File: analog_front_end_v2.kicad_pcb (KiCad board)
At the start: 4 copper layers, 153 parts, among them J1 Conn_Coaxial, J3 Conn_01x01_Socket, J4 Conn_01x01_Socket, U1 ADL5531, U10 PMOD 2x6, U11 LP2985-5.0, U12 LP2985-5.0, U13 LT1363, U14 MAX 735, U15 LP2985-2.5, U16 MAX889SESA, U17 MAX6102, U2 ADL5531, U3 ADL5531, U4 PE4140B-Z, U5 ADF4360-9, U6 LTC1406, U7 THS4551, U8 LT1363, U9 PMOD 2x6

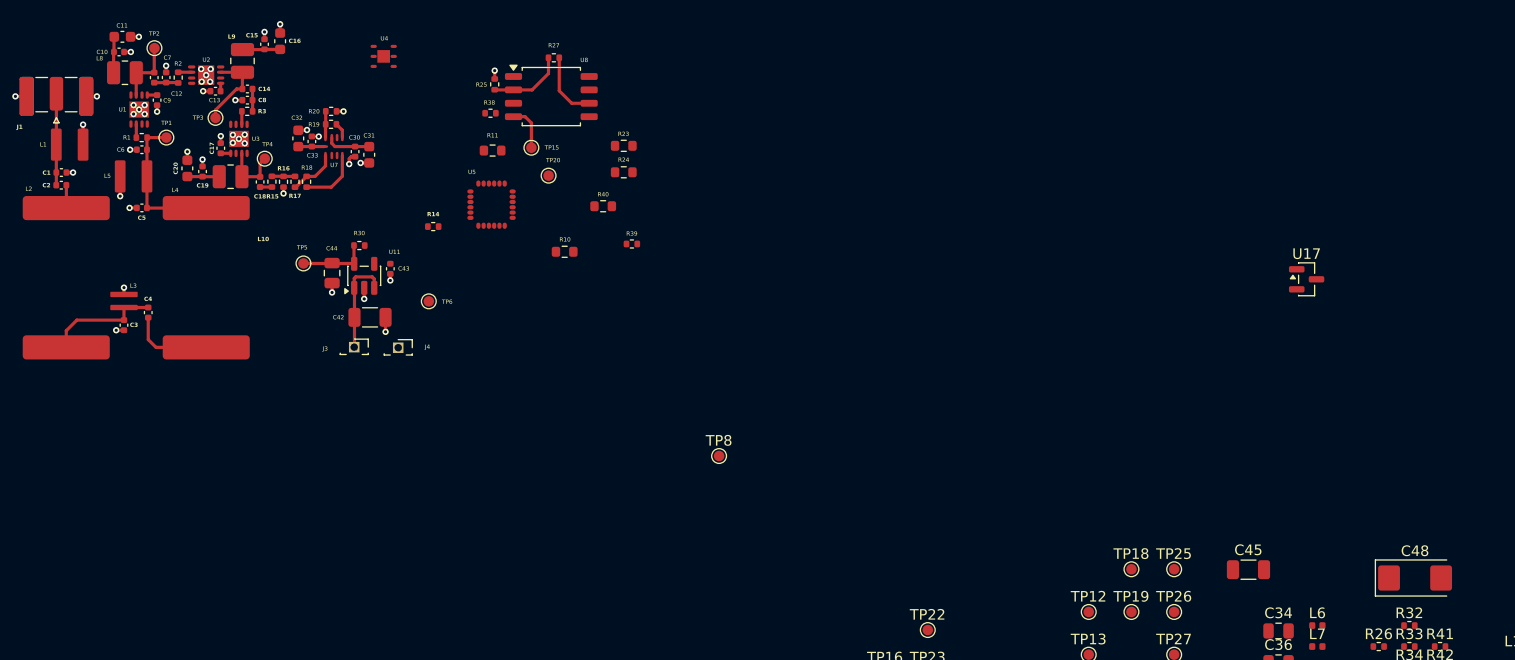
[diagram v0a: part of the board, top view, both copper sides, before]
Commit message: Routing for 5V_LNA and VIN connections. Also added note to add GND Planes for L2/L2
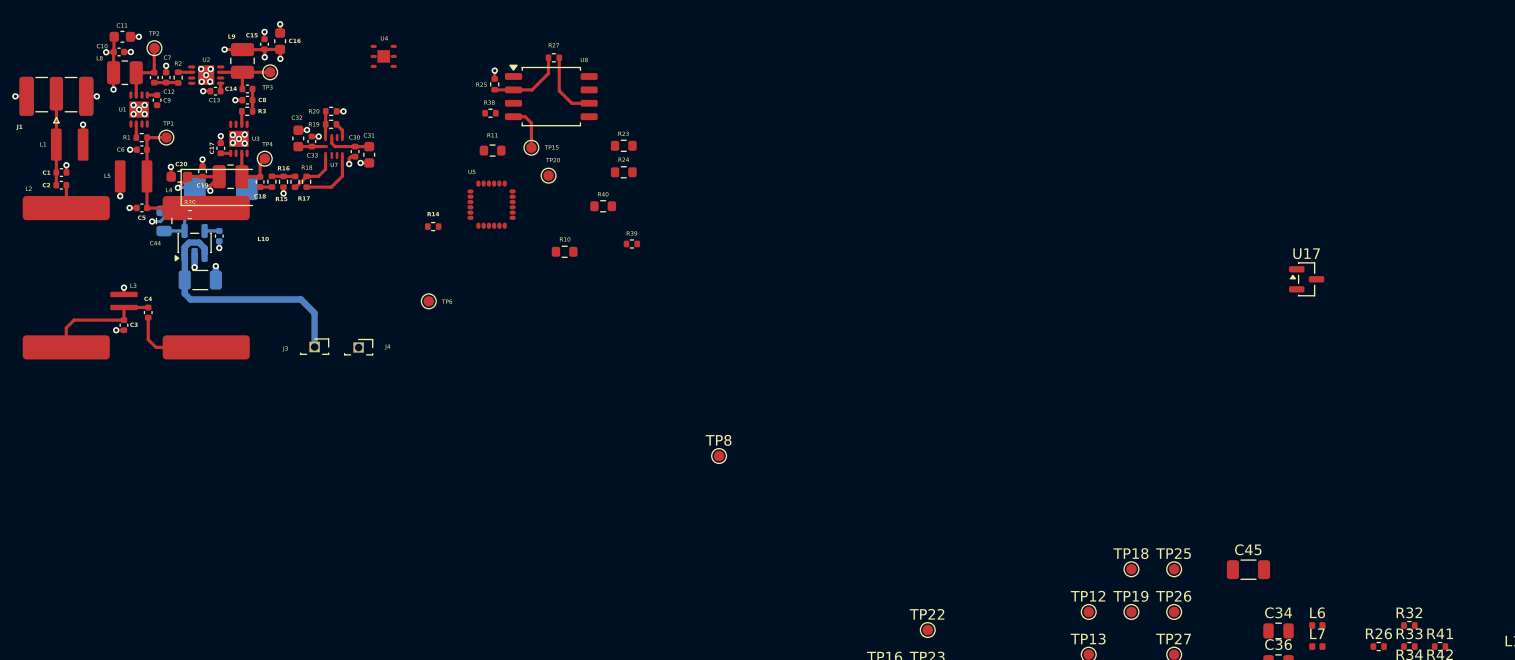
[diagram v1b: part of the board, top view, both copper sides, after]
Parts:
- removed TP5: ~, TestPoint:TestPoint_Pad_D1.0mm
- moved C48 119.2 mm to (32.8, 28.9)
- moved C44 16.7 mm to (27.4, 32.1), turned to -90 degrees
- moved C43 16.5 mm to (32.6, 33.5)
- moved C42 16.5 mm to (30.8, 37.7)
- moved U11 16.4 mm to (30.3, 34.1)
- moved R30 16.3 mm to (29.9, 31.5)
- moved TP3 6.74 mm to (37.5, 18.0)
- moved J3 3.76 mm to (41.7, 44.0)
- moved J4 3.76 mm to (45.9, 44.1)
- moved C20 1.10 mm to (28.9, 27.9), turned to 180 degrees
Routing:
- net 5V_LNA: track 10.0 -> 24.6 mm, vias 0 -> 7
- net VIN: track 9.47 -> 23.5 mm
- net Net-(U11-VOUT): track 6.59 -> 3.49 mm
- net Net-(U2-RFOUT): track 7.78 -> 6.28 mm
- net Net-(U11-BP): track 0.00 -> 1.38 mm
- net GND: track 27.0 -> 27.5 mm, vias 46 -> 45
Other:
- board text added: "TODO: Add solid GND planes on layers 2/3 Ground via stitching Decisions: Use 0.3mm trace for 50ohm characteristic impedance for microstrip with solid groundplane in layers 2,3 Use 0.4mm silkscreen width/height to balance readability/placement Ensure RF Mixer (U4) is far away from sensitive RF/analog front end"
- board text removed: "TODO: Ground via stitching Decisions: Use 0.3mm trace for 50ohm characteristic impedance for microstrip with solid groundplane in layers 2,3 Use 0.4mm silkscreen width/height to balance readability/placement Ensure RF Mixer (U4) is far away from sensitive RF/analog front end"

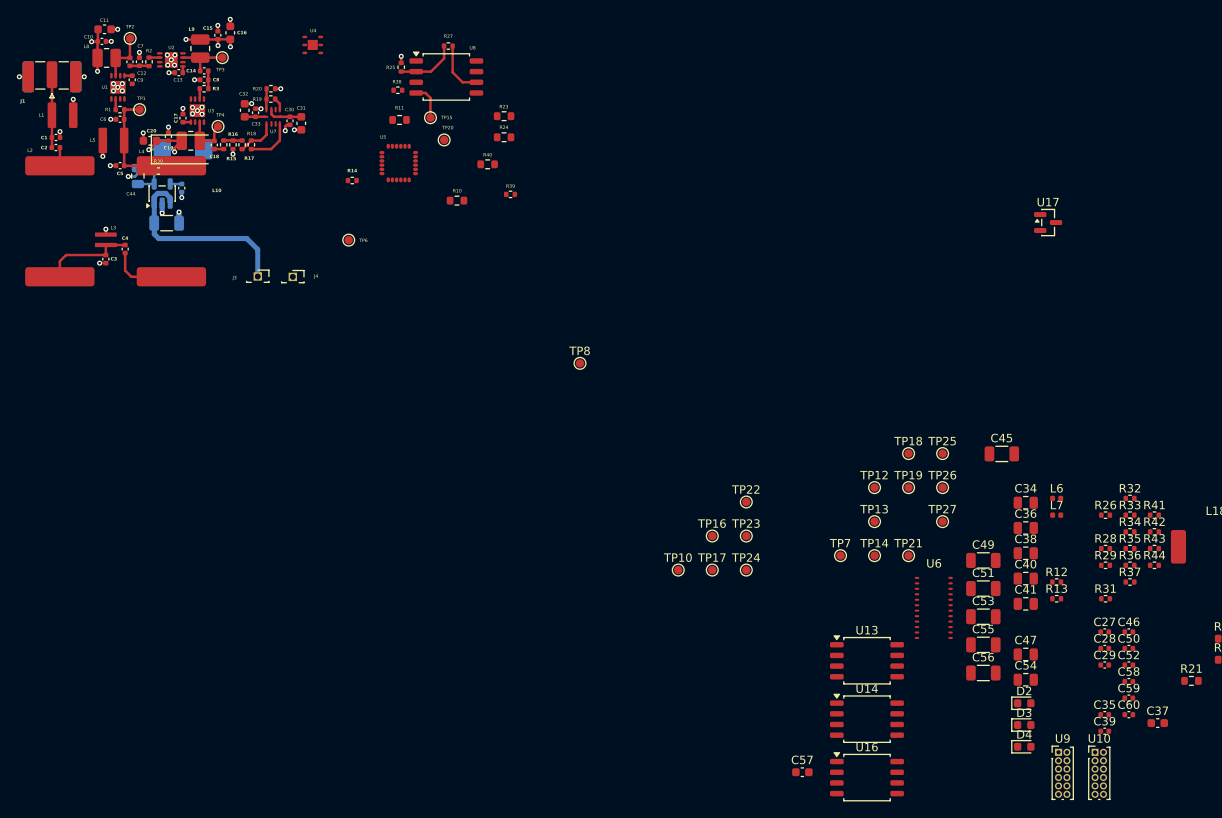
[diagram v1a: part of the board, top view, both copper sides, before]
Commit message: Further RF front end miniaturization
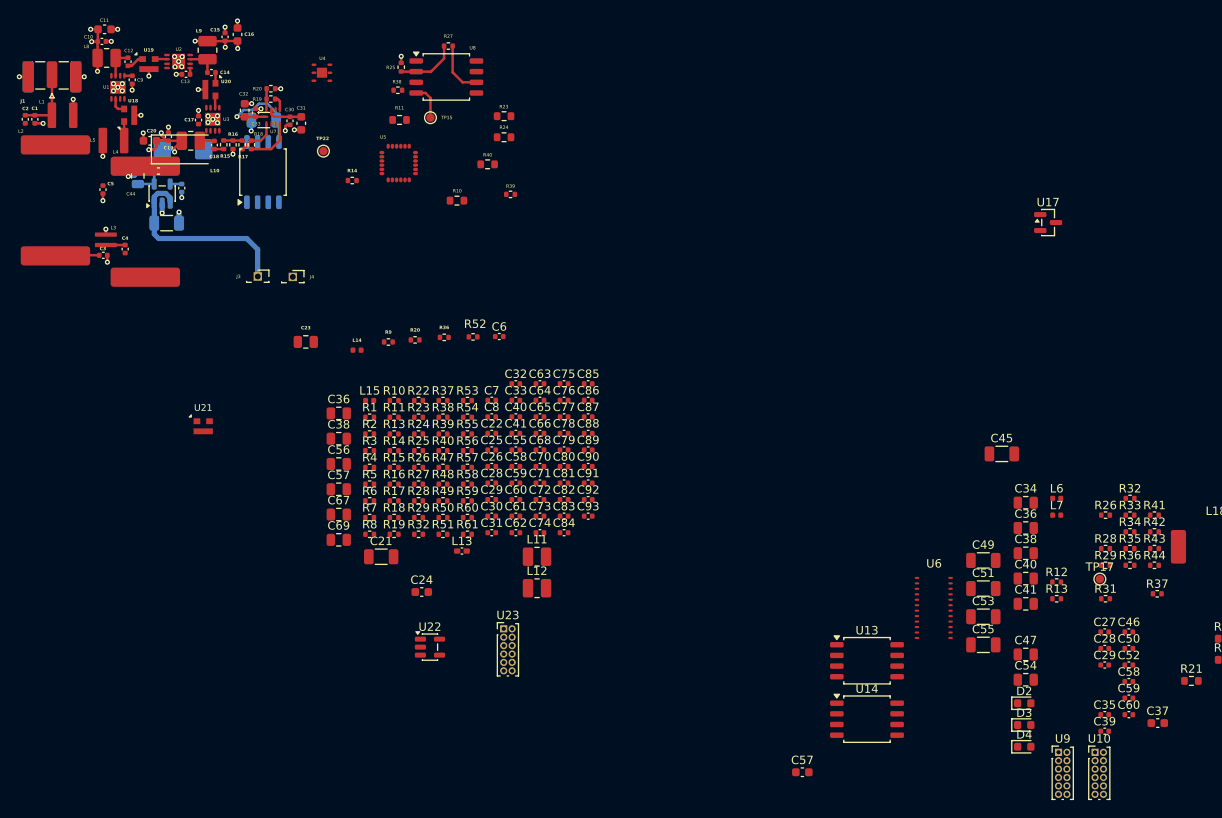
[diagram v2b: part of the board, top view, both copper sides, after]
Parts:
- removed TP1, TP10, TP12, TP13, TP14, TP18, TP19, TP2, TP20, TP21, TP23, TP24, TP25, TP26, TP3, TP4: TestPoint, TestPoint:TestPoint_Pad_D1.0mm
- removed TP16, TP27, TP6, TP7, TP8: ~, TestPoint:TestPoint_Pad_D1.0mm
- added C21: 10u_50V, Capacitor_SMD:C_1206_3216Metric, F.Cu at (56.4, 77.4)
- added C22: 10n_25V, Capacitor_SMD:C_0402_1005Metric, F.Cu at (69.5, 62.7)
- added C23: 10u_16V, Capacitor_SMD:C_0805_2012Metric, F.Cu at (47.4, 51.8)
- added C24: 1u_16V, Capacitor_SMD:C_0603_1608Metric, F.Cu at (61.2, 81.6)
- added C25: 1n_50V, Capacitor_SMD:C_0402_1005Metric, F.Cu at (69.5, 64.7)
- added C26: 1n_50V, Capacitor_SMD:C_0402_1005Metric, F.Cu at (69.5, 66.6)
- added C28: 100p_50V, Capacitor_SMD:C_0402_1005Metric, F.Cu at (69.5, 68.6)
- added C29: 100p_50V, Capacitor_SMD:C_0402_1005Metric, F.Cu at (69.5, 70.6)
- added C30: 1p5F, Capacitor_SMD:C_0402_1005Metric, F.Cu at (69.5, 72.5)
- added C31: 1p8F, Capacitor_SMD:C_0402_1005Metric, F.Cu at (69.5, 74.5)
- added C32: 22n_25V_COG, Capacitor_SMD:C_0402_1005Metric, F.Cu at (72.4, 56.8)
- added C33: 1u_16V, Capacitor_SMD:C_0402_1005Metric, F.Cu at (72.4, 58.8)
- added C36: 10u_16V, Capacitor_SMD:C_0805_2012Metric, F.Cu at (51.3, 60.3)
- added C38: 10u_16V, Capacitor_SMD:C_0805_2012Metric, F.Cu at (51.3, 63.3)
- added C40: 0.1uF, Capacitor_SMD:C_0402_1005Metric, F.Cu at (72.4, 60.7)
- added C41: 0.1uF, Capacitor_SMD:C_0402_1005Metric, F.Cu at (72.4, 62.7)
- added C55: 0.1uF, Capacitor_SMD:C_0402_1005Metric, F.Cu at (72.4, 64.7)
- added C56: 10u_16V, Capacitor_SMD:C_0805_2012Metric, F.Cu at (51.3, 66.3)
- added C57: 10u_16V, Capacitor_SMD:C_0805_2012Metric, F.Cu at (51.3, 69.3)
- added C58: 100n_25V, Capacitor_SMD:C_0402_1005Metric, F.Cu at (72.4, 66.6)
- added C59: 100n_25V, Capacitor_SMD:C_0402_1005Metric, F.Cu at (72.4, 68.6)
- added C60: 0.1uF, Capacitor_SMD:C_0402_1005Metric, F.Cu at (72.4, 70.6)
- added C61: 10p_50V, Capacitor_SMD:C_0402_1005Metric, F.Cu at (72.4, 72.5)
- added C62: 1u_16V, Capacitor_SMD:C_0402_1005Metric, F.Cu at (72.4, 74.5)
- added C63: 200p_50V, Capacitor_SMD:C_0402_1005Metric, F.Cu at (75.3, 56.8)
- added C64: 200p_50V, Capacitor_SMD:C_0402_1005Metric, F.Cu at (75.3, 58.8)
- added C65: 1u_16V, Capacitor_SMD:C_0402_1005Metric, F.Cu at (75.3, 60.7)
- added C66: 10p_50V, Capacitor_SMD:C_0402_1005Metric, F.Cu at (75.3, 62.7)
- added C67: 10u_16V, Capacitor_SMD:C_0805_2012Metric, F.Cu at (51.3, 72.4)
- added C68: 1u_16V, Capacitor_SMD:C_0402_1005Metric, F.Cu at (75.3, 64.7)
- added C69: 10u_16V, Capacitor_SMD:C_0805_2012Metric, F.Cu at (51.3, 75.4)
- added C70: 200p_50V, Capacitor_SMD:C_0402_1005Metric, F.Cu at (75.3, 66.6)
- added C71: 200p_50V, Capacitor_SMD:C_0402_1005Metric, F.Cu at (75.3, 68.6)
- added C72: 0.1uF, Capacitor_SMD:C_0402_1005Metric, F.Cu at (75.3, 70.6)
- added C73: 0.1uF, Capacitor_SMD:C_0402_1005Metric, F.Cu at (75.3, 72.5)
- added C74: 0.1uF, Capacitor_SMD:C_0402_1005Metric, F.Cu at (75.3, 74.5)
- added C75: 0.1uF, Capacitor_SMD:C_0402_1005Metric, F.Cu at (78.1, 56.8)
- added C76: 1u_16V, Capacitor_SMD:C_0402_1005Metric, F.Cu at (78.1, 58.8)
- added C77: 1u_16V, Capacitor_SMD:C_0402_1005Metric, F.Cu at (78.1, 60.7)
- added C78: 10p_50V, Capacitor_SMD:C_0402_1005Metric, F.Cu at (78.1, 62.7)
- added C79: 10p_50V, Capacitor_SMD:C_0402_1005Metric, F.Cu at (78.1, 64.7)
- added C80: 100n_25V, Capacitor_SMD:C_0402_1005Metric, F.Cu at (78.1, 66.6)
- added C81: 0.1uF, Capacitor_SMD:C_0402_1005Metric, F.Cu at (78.1, 68.6)
- added C82: 1u_16V, Capacitor_SMD:C_0402_1005Metric, F.Cu at (78.1, 70.6)
- added C83: 1u_16V, Capacitor_SMD:C_0402_1005Metric, F.Cu at (78.1, 72.5)
- added C84: 100n_25V, Capacitor_SMD:C_0402_1005Metric, F.Cu at (78.1, 74.5)
- added C85: 0.1uF, Capacitor_SMD:C_0402_1005Metric, F.Cu at (81.0, 56.8)
- added C86: 200p_50V, Capacitor_SMD:C_0402_1005Metric, F.Cu at (81.0, 58.8)
- added C87: 200p_50V, Capacitor_SMD:C_0402_1005Metric, F.Cu at (81.0, 60.7)
- added C88: 0.1uF, Capacitor_SMD:C_0402_1005Metric, F.Cu at (81.0, 62.7)
- added C89: 0.1uF, Capacitor_SMD:C_0402_1005Metric, F.Cu at (81.0, 64.7)
- added C90: 0.1uF, Capacitor_SMD:C_0402_1005Metric, F.Cu at (81.0, 66.6)
- added C91: 200p_50V, Capacitor_SMD:C_0402_1005Metric, F.Cu at (81.0, 68.6)
- added C92: 200p_50V, Capacitor_SMD:C_0402_1005Metric, F.Cu at (81.0, 70.6)
- added C93: 0.1uF, Capacitor_SMD:C_0402_1005Metric, F.Cu at (81.0, 72.5)
- added L11: 159n, Inductor_SMD:L_1008_2520Metric, F.Cu at (74.9, 77.4)
- added L12: 470n, Inductor_SMD:L_1008_2520Metric, F.Cu at (74.9, 81.1)
- added L13: 160n, Inductor_SMD:L_0402_1005Metric_Pad0.77x0.64mm_HandSolder, F.Cu at (66.0, 76.7)
- added L14: 72n, Inductor_SMD:L_0402_1005Metric, F.Cu at (53.5, 52.8)
- added L15: 72n, Inductor_SMD:L_0402_1005Metric, F.Cu at (55.0, 58.8)
- added R10: 0R, Resistor_SMD:R_0402_1005Metric, F.Cu at (57.9, 58.8)
- added R11: 20kR, Resistor_SMD:R_0402_1005Metric, F.Cu at (57.9, 60.8)
- added R13: 49k3R, Resistor_SMD:R_0402_1005Metric, F.Cu at (57.9, 62.8)
- added R14: 75kR, Resistor_SMD:R_0402_1005Metric, F.Cu at (57.9, 64.8)
- added R15: 4k22R, Resistor_SMD:R_0402_1005Metric, F.Cu at (57.9, 66.8)
- added R16: 8k2R, Resistor_SMD:R_0402_1005Metric, F.Cu at (57.9, 68.7)
- added R17: 2k43R, Resistor_SMD:R_0402_1005Metric, F.Cu at (57.9, 70.7)
- added R18: 24R9, Resistor_SMD:R_0402_1005Metric, F.Cu at (57.9, 72.7)
- added R19: 20kR, Resistor_SMD:R_0402_1005Metric, F.Cu at (57.9, 74.7)
- added R20: 4k22R, Resistor_SMD:R_0402_1005Metric, F.Cu at (60.4, 51.6)
- added R22: 49k3R, Resistor_SMD:R_0402_1005Metric, F.Cu at (60.8, 58.8)
- added R23: 75kR, Resistor_SMD:R_0402_1005Metric, F.Cu at (60.8, 60.8)
- added R24: 8k2R, Resistor_SMD:R_0402_1005Metric, F.Cu at (60.8, 62.8)
- added R25: 24R9, Resistor_SMD:R_0402_1005Metric, F.Cu at (60.8, 64.8)
- added R26: 100R, Resistor_SMD:R_0402_1005Metric, F.Cu at (60.8, 66.8)
- added R27: 2k43R, Resistor_SMD:R_0402_1005Metric, F.Cu at (60.8, 68.7)
- added R28: 20kR, Resistor_SMD:R_0402_1005Metric, F.Cu at (60.8, 70.7)
- added R29: 20kR, Resistor_SMD:R_0402_1005Metric, F.Cu at (60.8, 72.7)
- added R32: 100R, Resistor_SMD:R_0402_1005Metric, F.Cu at (60.8, 74.7)
- added R36: 100R, Resistor_SMD:R_0402_1005Metric, F.Cu at (63.9, 51.3)
- added R37: 100R, Resistor_SMD:R_0402_1005Metric, F.Cu at (63.7, 58.8)
- added R38: 4k22R, Resistor_SMD:R_0402_1005Metric, F.Cu at (63.7, 60.8)
- added R39: 4k22R, Resistor_SMD:R_0402_1005Metric, F.Cu at (63.7, 62.8)
- added R4: 50R, Resistor_SMD:R_0402_1005Metric, F.Cu at (55.0, 66.8)
- added R40: 49k3R, Resistor_SMD:R_0402_1005Metric, F.Cu at (63.7, 64.8)
- added R47: 49k3R, Resistor_SMD:R_0402_1005Metric, F.Cu at (63.7, 66.8)
- added R48: 75kR, Resistor_SMD:R_0402_1005Metric, F.Cu at (63.7, 68.7)
- added R49: 75kR, Resistor_SMD:R_0402_1005Metric, F.Cu at (63.7, 70.7)
- added R5: 0R, Resistor_SMD:R_0402_1005Metric, F.Cu at (55.0, 68.7)
- added R50: 8k2R, Resistor_SMD:R_0402_1005Metric, F.Cu at (63.7, 72.7)
- added R51: 24R9, Resistor_SMD:R_0402_1005Metric, F.Cu at (63.7, 74.7)
- added R52: 8k2R, Resistor_SMD:R_0402_1005Metric, F.Cu at (67.3, 51.2)
- added R53: 24R9, Resistor_SMD:R_0402_1005Metric, F.Cu at (66.6, 58.8)
- added R54: 2k43R, Resistor_SMD:R_0402_1005Metric, F.Cu at (66.6, 60.8)
- added R55: 2k43R, Resistor_SMD:R_0402_1005Metric, F.Cu at (66.6, 62.8)
- added R56: 100R, Resistor_SMD:R_0402_1005Metric, F.Cu at (66.6, 64.8)
- added R57: 100R, Resistor_SMD:R_0402_1005Metric, F.Cu at (66.6, 66.8)
- added R58: 100R, Resistor_SMD:R_0402_1005Metric, F.Cu at (66.6, 68.7)
- added R59: 100R, Resistor_SMD:R_0402_1005Metric, F.Cu at (66.6, 70.7)
- added R6: 240R, Resistor_SMD:R_0402_1005Metric, F.Cu at (55.0, 70.7)
- added R60: 100R, Resistor_SMD:R_0402_1005Metric, F.Cu at (66.6, 72.7)
- added R61: 100R, Resistor_SMD:R_0402_1005Metric, F.Cu at (66.6, 74.7)
- added R7: 49R9, Resistor_SMD:R_0402_1005Metric, F.Cu at (55.0, 72.7)
- added R8: 49R9, Resistor_SMD:R_0402_1005Metric, F.Cu at (55.0, 74.7)
- added R9: 0R, Resistor_SMD:R_0402_1005Metric, F.Cu at (57.2, 51.8)
- added U18: PAT1220-C-0DB, RF_Converter:RF_Attenuator_Susumu_PAT1220, F.Cu at (26.4, 24.8)
- added U19: PAT1220-C-0DB, RF_Converter:RF_Attenuator_Susumu_PAT1220, F.Cu at (28.7, 18.7)
- added U20: PAT1220-C-0DB, RF_Converter:RF_Attenuator_Susumu_PAT1220, F.Cu at (36.0, 21.8)
- added U21: PAT1220-C-0DB, RF_Converter:RF_Attenuator_Susumu_PAT1220, F.Cu at (35.2, 61.9)
- added U22: LP2985-3.3, Package_TO_SOT_SMD:SOT-23-5, F.Cu at (62.2, 88.1)
- added U23: PMOD 2x6, Connector_PinHeader_1.00mm:PinHeader_2x06_P1.00mm_Vertical, F.Cu at (71.0, 86.0)
- C6: value 5p1_50V -> 220pF
- C7, C8: value 5p1_50V -> 15.9pF
- R2: value 0R -> 20kR
- R3: value 0R -> 50R
- moved C56 108.0 mm to (42.4, 25.4), turned to 180 degrees
- moved U16 101.8 mm to (42.3, 31.6), turned to 90 degrees
- moved TP22 65.4 mm to (49.5, 29.1)
- moved C7 58.2 mm to (69.5, 58.8), turned to 0 degrees
- moved C8 52.7 mm to (69.5, 60.7), turned to 0 degrees
- moved C6 52.0 mm to (70.4, 51.2), turned to 0 degrees
- moved R2 51.5 mm to (55.0, 62.8), turned to 0 degrees
- moved R3 47.4 mm to (55.0, 64.8), turned to 0 degrees
- moved R1 47.2 mm to (55.0, 60.8), turned to 0 degrees
- moved TP17 46.1 mm to (141.9, 80.0)
- moved C2 4.96 mm to (14.0, 25.3), turned to 90 degrees
- moved R37 3.53 mm to (148.8, 81.8)
- moved C5 3.50 mm to (23.3, 33.7), turned to -90 degrees
- moved U4 3.48 mm to (49.3, 19.8)
- moved C1 3.32 mm to (15.2, 25.3), turned to -90 degrees
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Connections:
- C6 pad 1: Net-(C5-Pad1) -> Net-(C6-Pad1)
- C6 pad 2: GND -> Net-(C6-Pad2)
- C7 pad 1: Net-(C12-Pad2) -> Net-(C6-Pad2)
- C8 pad 1: Net-(C14-Pad2) -> GND
- C8 pad 2: GND -> Net-(U7-IF+)
- R1 pad 1: Net-(C5-Pad1) -> Net-(U22-VOUT)
- R1 pad 2: Net-(U1-RFIN) -> 3.3V
- R2 pad 1: Net-(C12-Pad2) -> Net-(U7-EN)
- R2 pad 2: Net-(U2-RFIN) -> 3.3V
- R21 pad 1: 2.5V_DiffAmp -> 2V5_ADC
- R3 pad 1: Net-(C14-Pad2) -> DEMOD_VCTRL
- R3 pad 2: Net-(U3-RFIN) -> Net-(R3-Pad2)
- R35 pad 2: 2.5V_DiffAmp -> 2V5_ADC
- U5 pad 4: Net-(U5-RFOUTA) -> 3.3V_PMOD
- U5 pad 5: Net-(U5-RFOUTB) -> 3.3V_PMOD
- U9 pad 1: Net-(U6-CLK) -> unconnected-(U9-Pad1)
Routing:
- net Net-(C5-Pad1): track 14.2 -> 2.27 mm
- net -2.5V_DiffAmp: track 2.48 -> 12.3 mm, vias 0 -> 1
- net Net-(C4-Pad2): track 7.89 -> 0.00 mm
- net Net-(C3-Pad1): track 11.1 -> 4.42 mm
- net Net-(U3-RFOUT): track 5.61 -> 1.73 mm
- net GND: track 27.5 -> 30.5 mm, vias 45 -> 47
- net Net-(U2-RFOUT): track 6.28 -> 3.66 mm
- net Net-(U1-RFOUT): track 6.15 -> 3.60 mm
- net 5V_LNA: track 24.6 -> 27.0 mm, vias 7 -> 9
- net Net-(C2-Pad1): track 2.17 -> 0.00 mm
- net Net-(U3-CLIN): track 0.95 -> 0.00 mm
- net Net-(C14-Pad2): track 2.15 -> 1.28 mm
- net Net-(U1-RFIN): track 1.29 -> 2.06 mm
- net Net-(J1-In): track 8.69 -> 8.01 mm
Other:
- board text added: "12V lithium ion battery / or DC IN from benchtop power supply and GND"
- board text removed: "12V DC IN from benchtop power supply and GND"
